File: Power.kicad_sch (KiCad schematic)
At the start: 53 parts, among them J16 19V 5A DC, Q2 AON7403, Q3 AON7403, Q4 AON7403, SW1 SW_Push, U11 LM3489MMX/NOPB, U6 LM3489MMX/NOPB, U8 LM3489MMX/NOPB

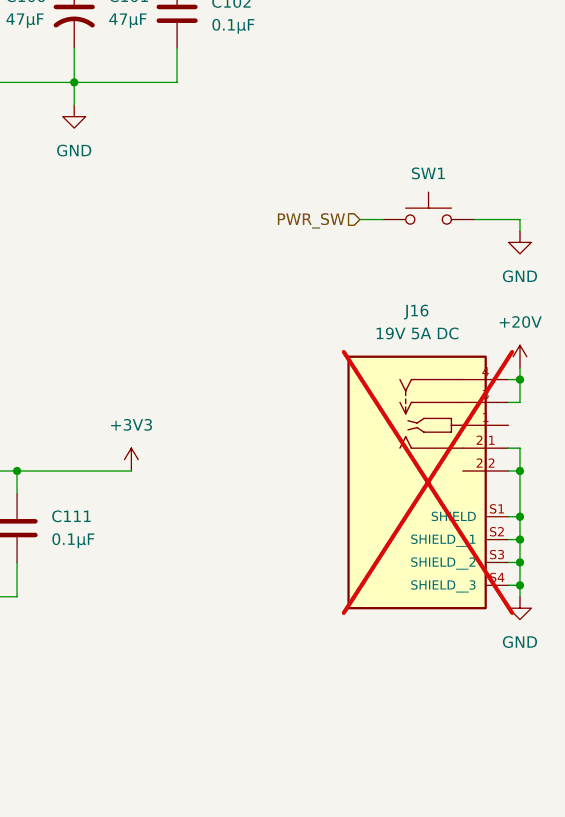
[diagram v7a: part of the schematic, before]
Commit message: pcb: replaced 20P slot with mirrored connector
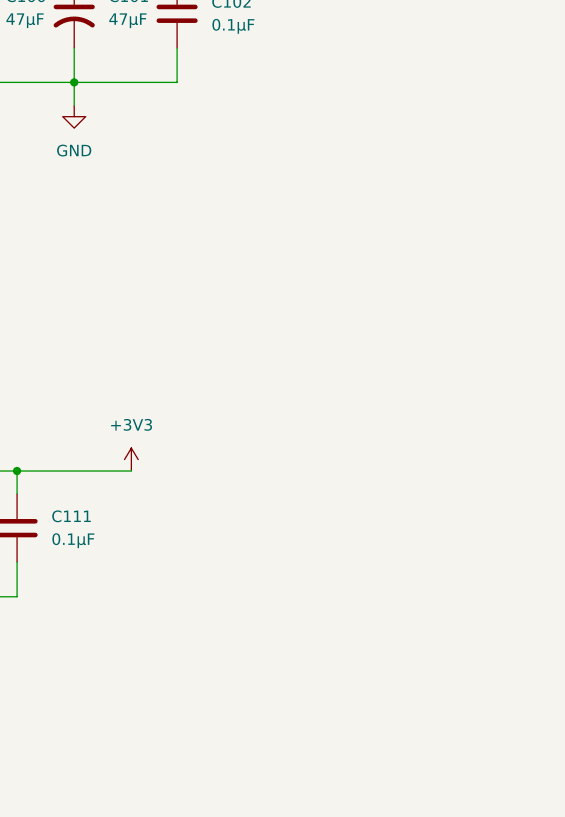
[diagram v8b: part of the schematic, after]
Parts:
- removed J16: 19V 5A DC, PJ-096H:CUI_PJ-096H, symbol PJ-096H:PJ-096H
- removed SW1: SW_Push, Button_Switch_SMD:SW_SPST_SKQG_WithStem, symbol Switch:SW_Push
